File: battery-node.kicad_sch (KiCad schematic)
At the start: 13 parts, among them J2 Conn_01x02, J3 Conn_01x02, J5 Conn_01x05, U1 ESP32-H2-MINI-1-H2S

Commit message: adding diode or
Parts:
- removed TP1: IO8, TestPoint:TestPoint_Pad_D1.0mm, symbol Connector:TestPoint
- added J7: TC2050, Connector:Tag-Connect_TC2050-IDC-NL_2x05_P1.27mm_Vertical, symbol Connector:TC2050
- added JP5: Jumper_2_Open, Jumper:SolderJumper-2_P1.3mm_Open_RoundedPad1.0x1.5mm, symbol Jumper:Jumper_2_Open
- added R56, R57, R61, R63, R64, R65: 33Ω, PCM_JLCPCB:R_0402, symbol PCM_JLCPCB-Resistors:0402,33Ω
- added TP6: IO9, symbol Connector:TestPoint
- TP3: value IO25 -> IO9
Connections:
- net +3V3: now also U1.8 (EN), JP5.1 (A)
- net DBG_MTCK: now also R57.1; no longer J5.3 (Pin_3)
- net DBG_MTDI: now also R63.1; no longer J5.2 (Pin_2)
- net DBG_MTDO: now also R61.1; no longer J5.4 (Pin_4)
- net DBG_MTMS: now also R56.1; no longer J5.5 (Pin_5)
- net GND: now also R64.2
- net ISOLATED_COMMS/CAN_SLEEP: now reaches U1.22 (IO8/BOOT0)
- net ISOLATED_COMMS/CAN_SLEEP: now also TP6.1
- net ISOLATED_COMMS/CAN_SHUTDOWN: now reaches TP3.1, U1.25 (IO25/BOOT2)
- net ISOLATED_COMMS/nEN_ISO_PWR renamed ISOLATED_COMMS/EN_ISO_PWR
- new net: J7.10, R56.2
- new net: JP5.2 (B), R65.2
- new net: J7.1, R65.1
- new net: J7.2, J7.3, J7.4, J7.5, R64.1
- new net: J7.7, R63.2
- new net: J7.8, R61.2
- new net: J7.9, R57.2
- no-connect marks 1 -> 2
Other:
- sheet ISOLATED_COMMS ports: added CAN_SHUTDOWN, CAN_SLEEP, EN_ISO_PWR; removed nEN_ISO_PWR
- moved on the sheet: J5, TP4, TP5

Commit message: rolled back TO commit caa5444, didn't mean to roll THAT back
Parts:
- removed J5: Conn_01x05, symbol Connector_Generic:Conn_01x05
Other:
- note added: "falling interrupt"
- note removed: "interrupt"
- moved on the sheet: J7, JP5, R56, R57, R61, R63, R64, R65, TP4, TP5

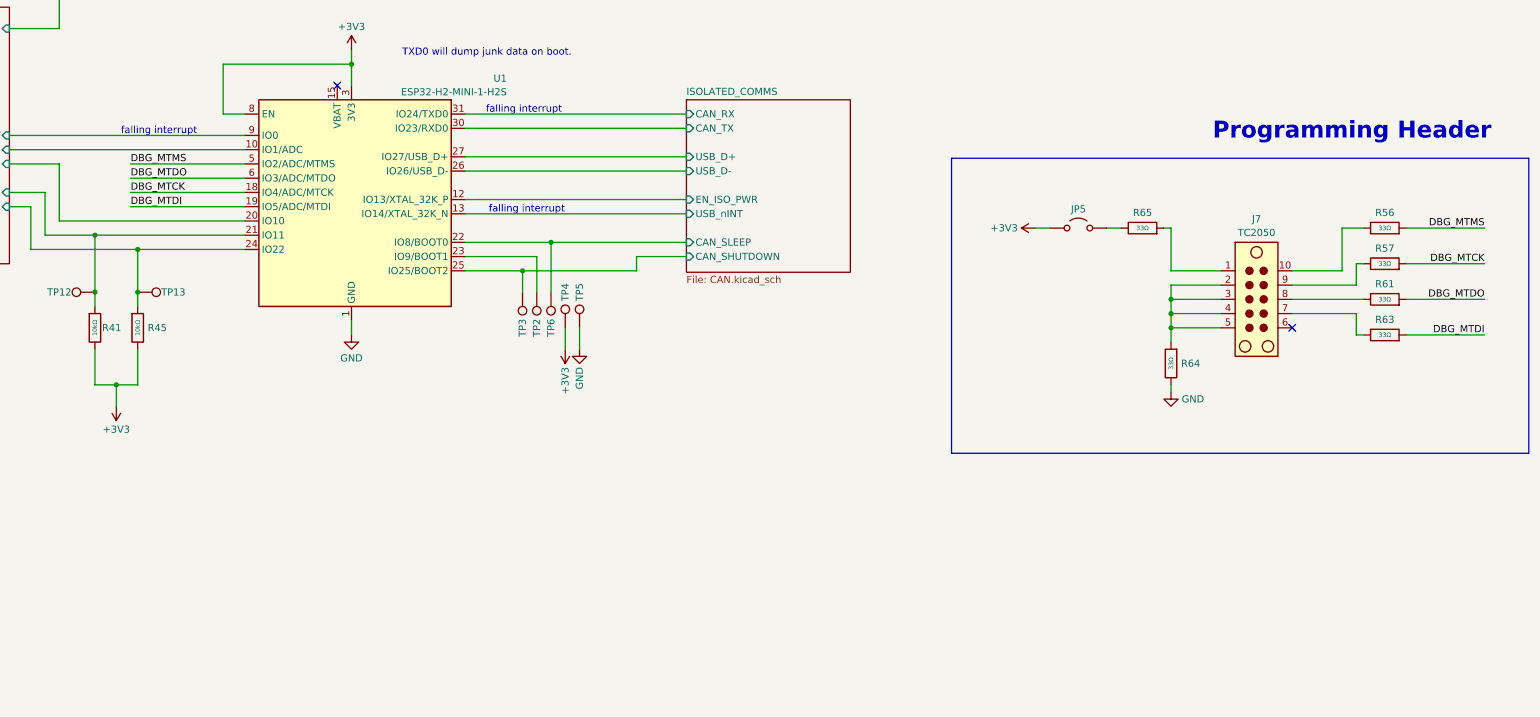
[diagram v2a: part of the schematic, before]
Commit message: Revert "added precharge circuit, filled in placeholder parts"
This reverts commit caa5444a50fe9d2ccb2e95970e40619801e9f697.
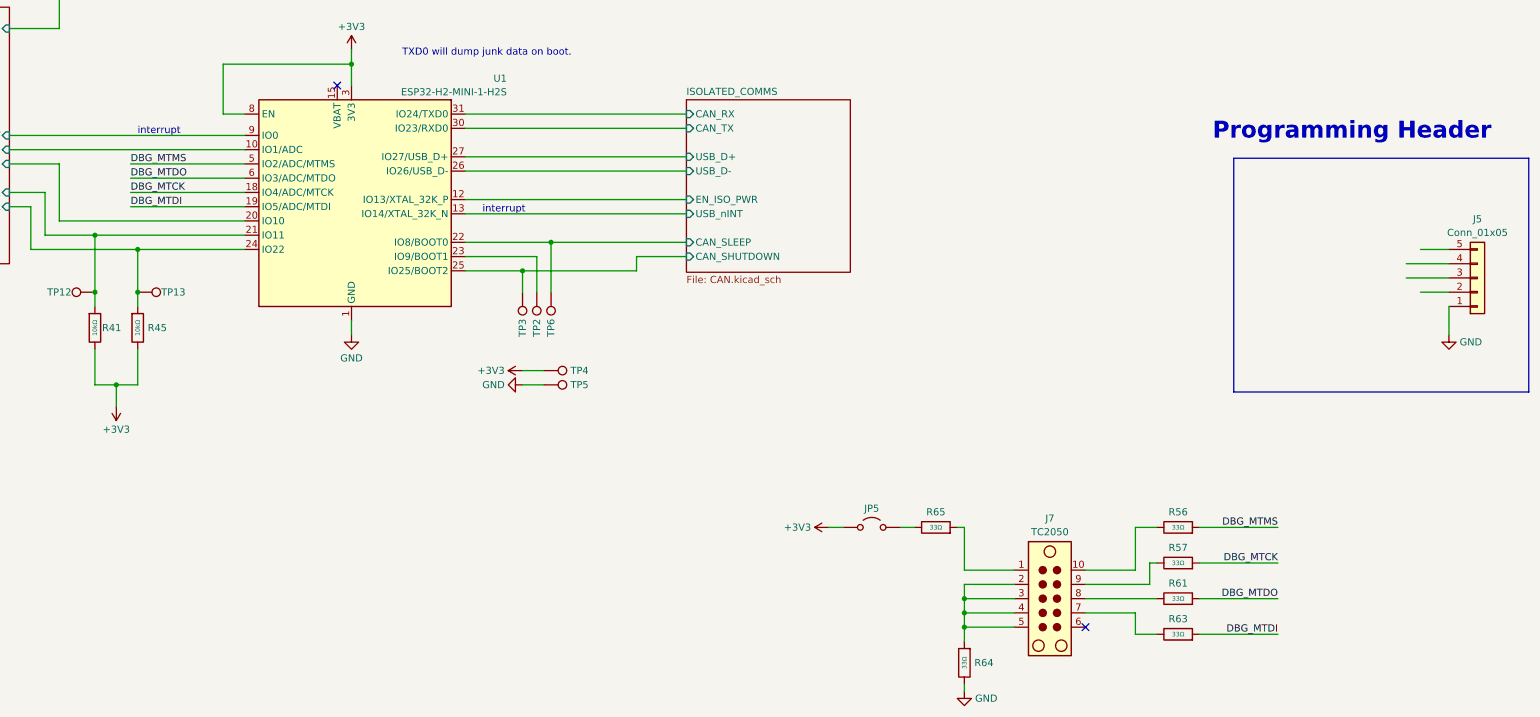
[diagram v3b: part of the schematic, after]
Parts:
- added J5: Conn_01x05, symbol Connector_Generic:Conn_01x05
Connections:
- net GND: now also J5.1 (Pin_1)
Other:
- note added: "interrupt"
- note removed: "falling interrupt"
- moved on the sheet: J7, JP5, R56, R57, R61, R63, R64, R65, TP4, TP5
